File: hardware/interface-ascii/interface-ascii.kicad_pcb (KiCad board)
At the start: 2 copper layers, 88.9 x 132.1 mm, 48 parts, among them J1 Apple 2, J2 Apple 1, J3 UART, J4 Conn_01x05, J5 ISP header, J6 Keyboard, J7 SOL-20, SW1 Options, U1 ATmega328P, U2 74LS166, U3 74LS138, U4 74LS138, U5 74LS04

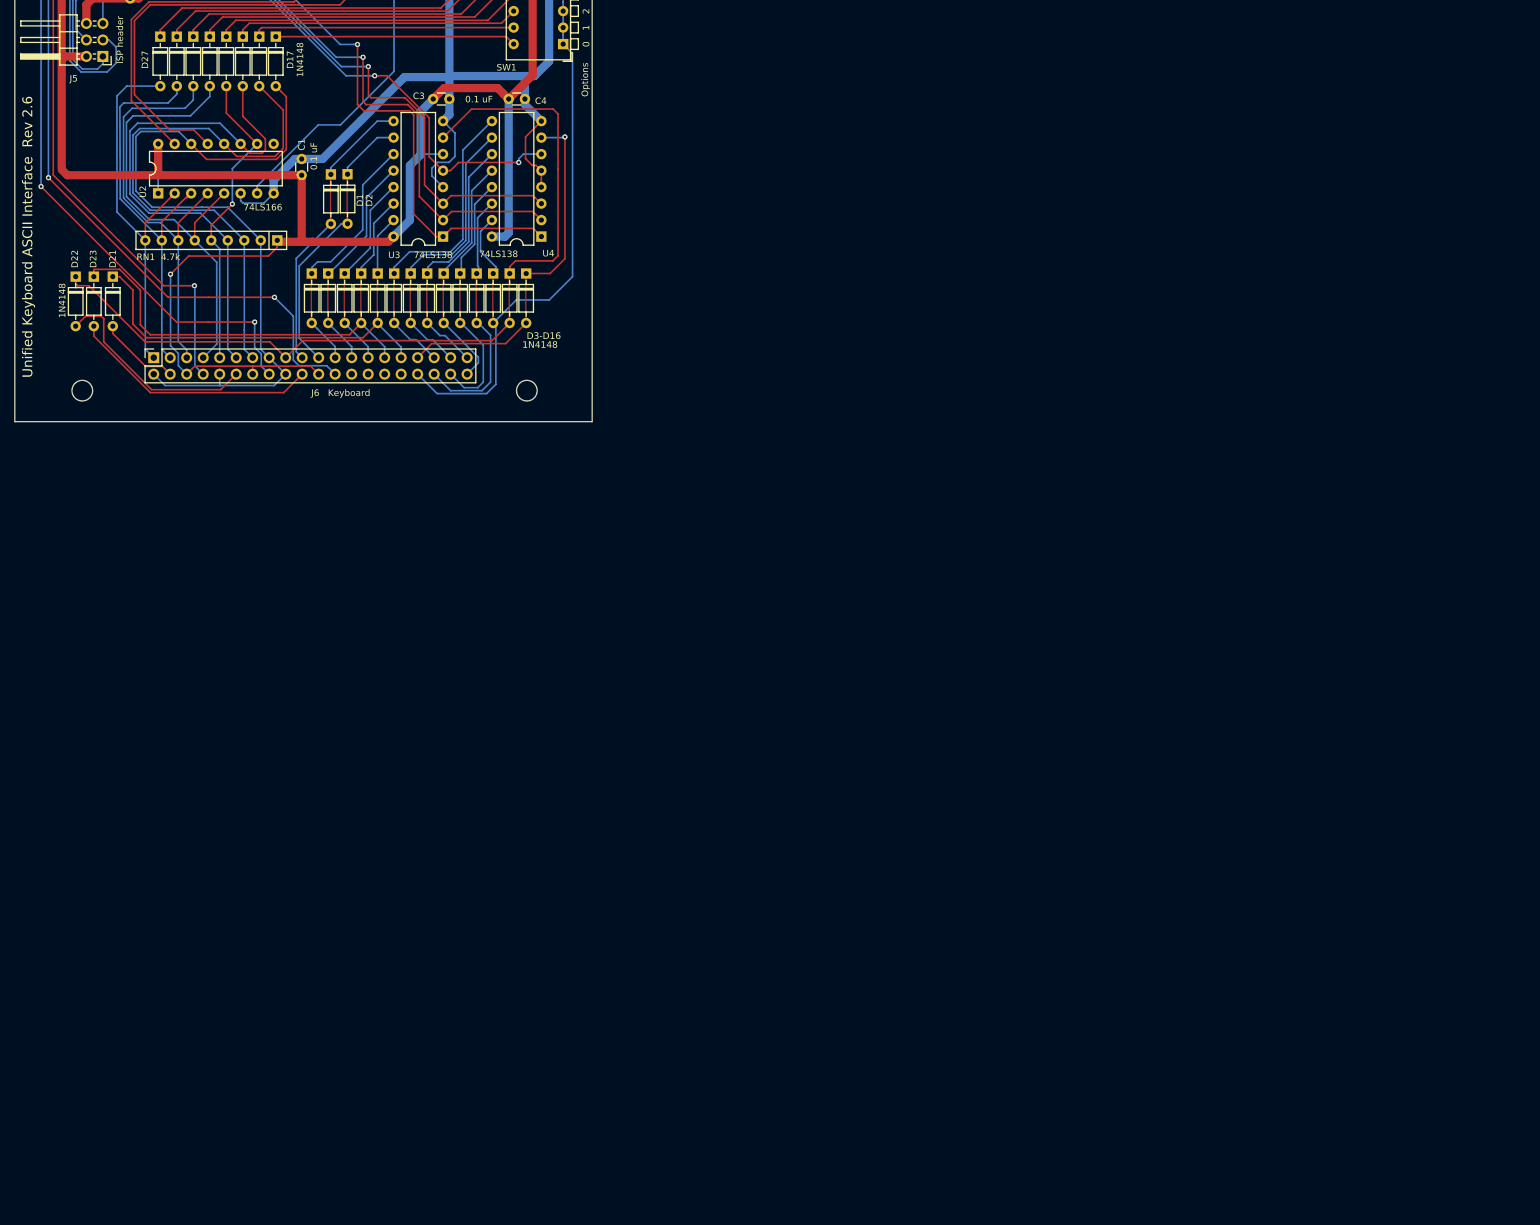
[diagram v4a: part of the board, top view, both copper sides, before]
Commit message: Cleanups on ASCII interface PCBs, 328P and 2560 versions
- Clean up diode positioning and numbering
- Remove 3D models for devices that are not normally fitted
- clean up labeling
- update README files to match PCBs.
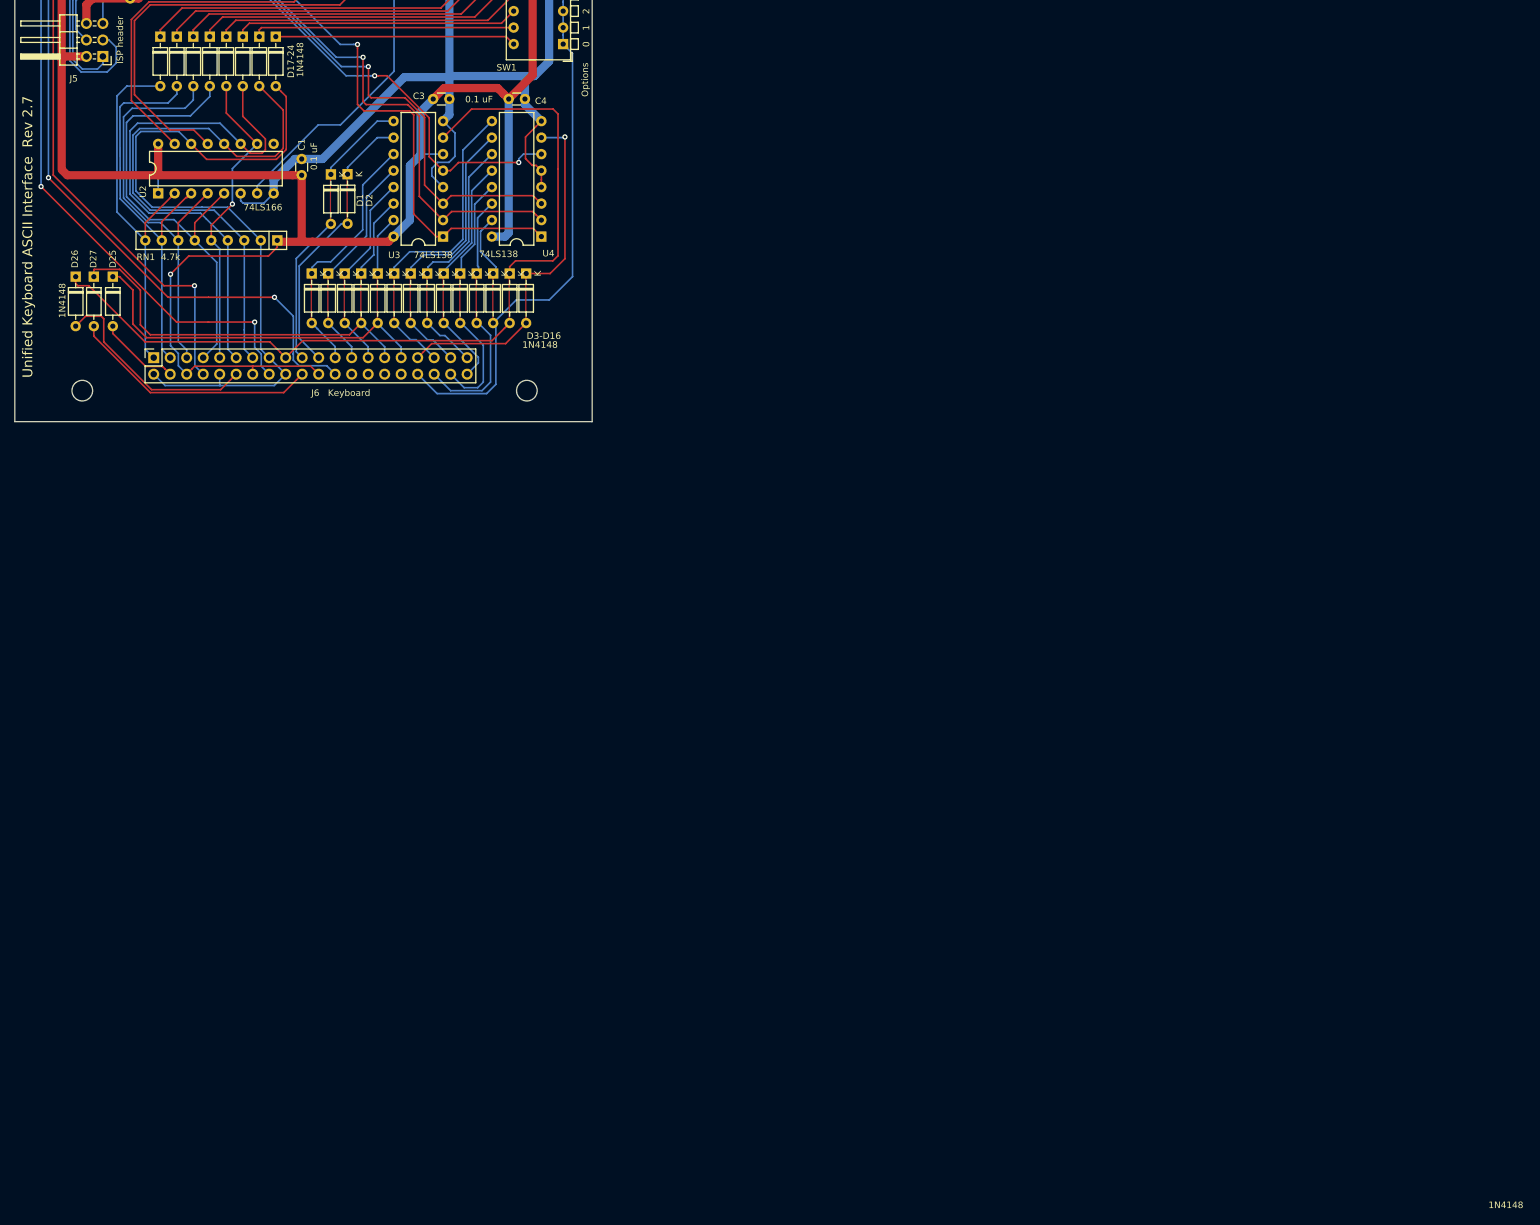
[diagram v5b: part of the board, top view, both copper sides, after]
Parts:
- added ?: , , F.Cu at (207.7, 128.6)
- renumbered D24 to D21, D25 to D22, D26 to D23, D27 to D24, D21 to D25, D22 to D26, D23 to D27
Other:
- board text added: "D17-24"
- board text added: "Unified Keyboard ASCII Interface Rev 2.7"
- board text removed: "Unified Keyboard ASCII Interface Rev 2.6"
